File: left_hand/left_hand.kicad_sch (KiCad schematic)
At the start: 4 parts, among them M1 Motor_Servo, Q1 Q_NMOS_GDS, U1 MCP23017_SP

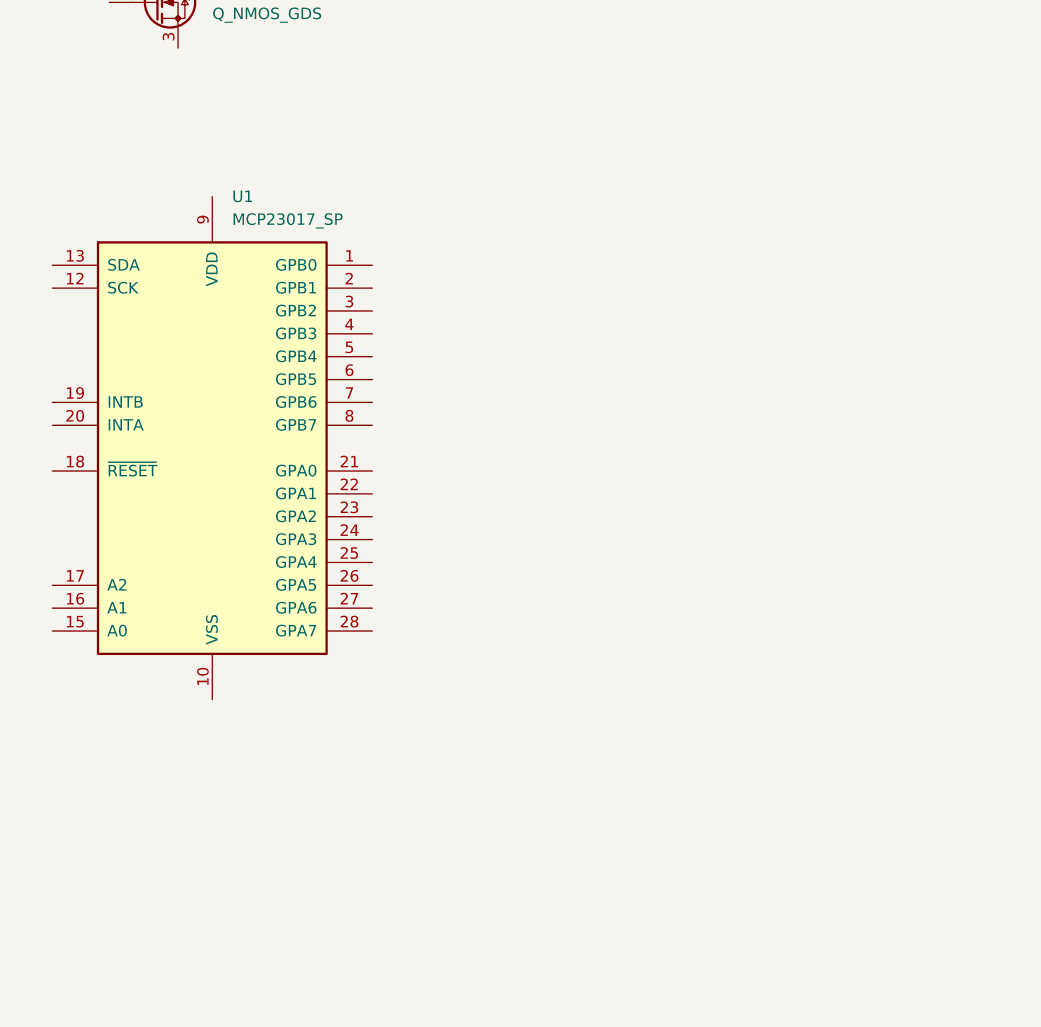
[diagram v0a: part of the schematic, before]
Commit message: Added PCA9615 differential I2C buffer
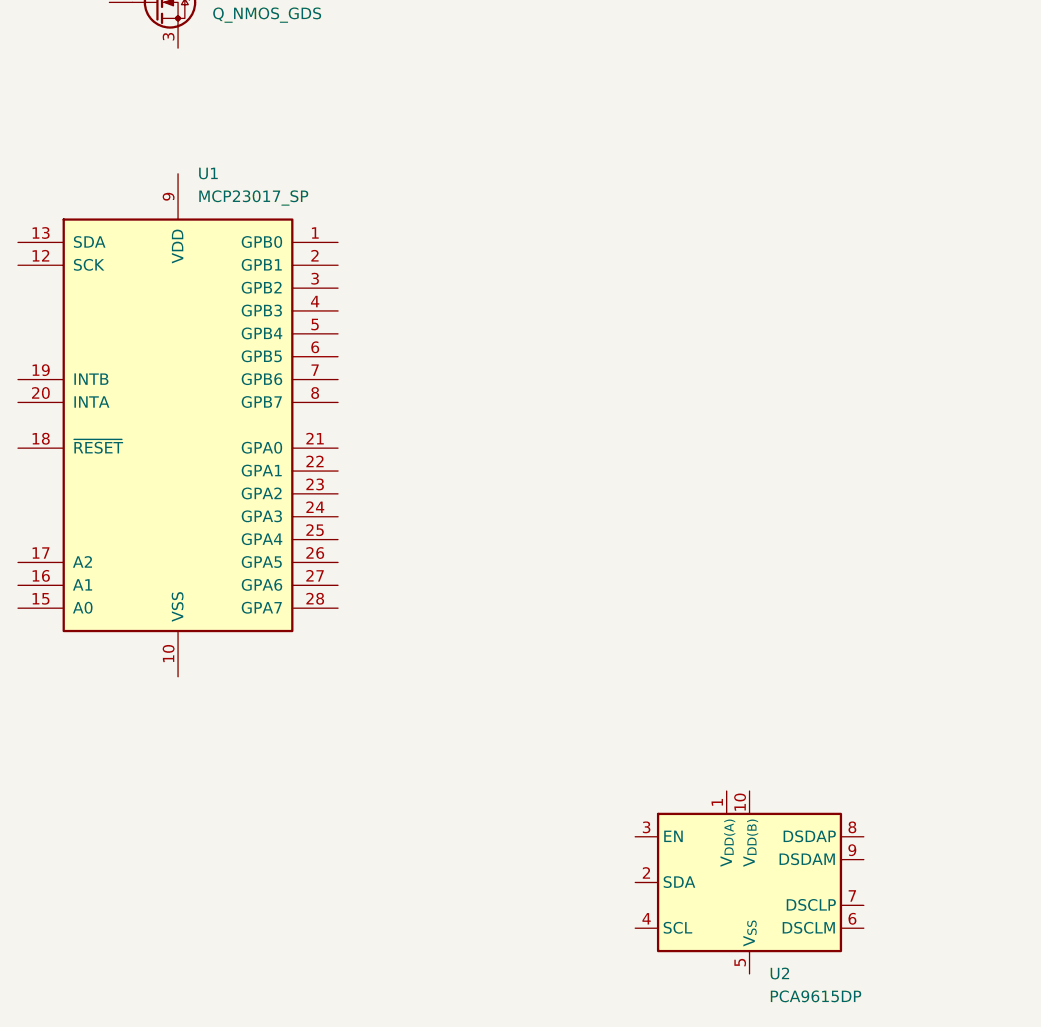
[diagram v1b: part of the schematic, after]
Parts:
- added U2: PCA9615DP, Package_SO:TSSOP-10_3x3mm_P0.5mm, symbol Interface:PCA9615DP
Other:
- moved on the sheet: U1
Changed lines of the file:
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@@
 	(symbol
 		(lib_id "Interface_Expansion:MCP23017_SP")
-		(at 63.5 118.11 0)
+		(at 59.69 115.57 0)
 		(unit 1)
 		(exclude_from_sim no)
@@
 		(fields_autoplaced yes)
 		(property "Reference" "U1"
-			(at 65.6941 90.17 0)
+			(at 61.8841 87.63 0)
 			(effects
 				(font
@@
 		)
 		(property "Value" "MCP23017_SP"
-			(at 65.6941 92.71 0)
+			(at 61.8841 90.17 0)
 			(effects
 				(font
@@
 		)
 		(property "Footprint" "Package_DIP:DIP-28_W7.62mm"
-			(at 68.58 143.51 0)
+			(at 64.77 140.97 0)
 			(effects
 				(font
@@
 		)
 		(property "Datasheet" "http://ww1.microchip.com/downloads/en/DeviceDoc/20001952C.pdf"
-			(at 68.58 146.05 0)
+			(at 64.77 143.51 0)
 			(effects
 				(font
@@
 		)
 		(property "Description" "16-bit I/O expander, I2C, interrupts, w pull-ups, SPDIP-28"
-			(at 63.5 118.11 0)
+			(at 59.69 115.57 0)
 			(effects
 				(font
@@
 		)
 		(property "Digikey" "https://www.digikey.ca/en/products/detail/microchip-technology/MCP23017-E-SP/894272"
-			(at 63.5 118.11 0)
+			(at 59.69 115.57 0)
 			(effects
 				(font
@@
 					(unit 1)
 				)
+			)
+		)
+	)
+	(symbol
+		(lib_id "Interface:PCA9615DP")
+		(at 123.19 166.37 0)
+		(unit 1)
+		(exclude_from_sim no)
+		(in_bom yes)
+		(on_board yes)
+		(dnp no)
+		(fields_autoplaced yes)
+		(property "Reference" "U2"
+			(at 125.3841 176.53 0)
+			(effects
+				(font
+					(size 1.27 1.27)
+				)
+				(justify left)
+			)
+		)
+		(property "Value" "PCA9615DP"
+			(at 125.3841 179.07 0)
+			(effects
+				(font
+					(size 1.27 1.27)
+				)
+				(justify left)
+			)
+		)
+		(property "Footprint" "Package_SO:TSSOP-10_3x3mm_P0.5mm"
+			(at 143.51 175.26 0)
+			(effects
+				(font
+					(size 1.27 1.27)
+				)
+				(hide yes)
+			)
+		)
+		(property "Datasheet" "https://www.nxp.com/docs/en/data-sheet/PCA9615.pdf"
+			(at 123.19 177.8 0)
+			(effects
+				(font
+					(size 1.27 1.27)
+				)
+				(hide yes)
+			)
+		)
+		(property "Description" "Dual bidirectional hot-swap multipoint bus buffer, SO-8"
+			(at 123.19 166.37 0)
+			(effects
+				(font
+					(size 1.27 1.27)
+				)
+				(hide yes)
+			)
+		)
+		(property "Digikey" "https://www.digikey.ca/en/products/detail/nxp-usa-inc/PCA9615DPZ/14635231"
+			(at 123.19 166.37 0)
+			(effects
+				(font
+					(size 1.27 1.27)
+				)
+				(hide yes)
+			)
+		)
+		(pin "9"
+		)
+		(pin "2"
+		)
+		(pin "4"
+		)
+		(pin "7"
+		)
+		(pin "10"
+		)
+		(pin "6"
+		)
+		(pin "3"
+		)
+		(pin "5"
+		)
+		(pin "1"
+		)
+		(pin "8"
+		)
+		(instances
+			(project ""
+				(path "/22d0e2d6-ca63-4bde-b22b-39e933f56b8a"
+					(reference "U2")
+					(unit 1)
+				)

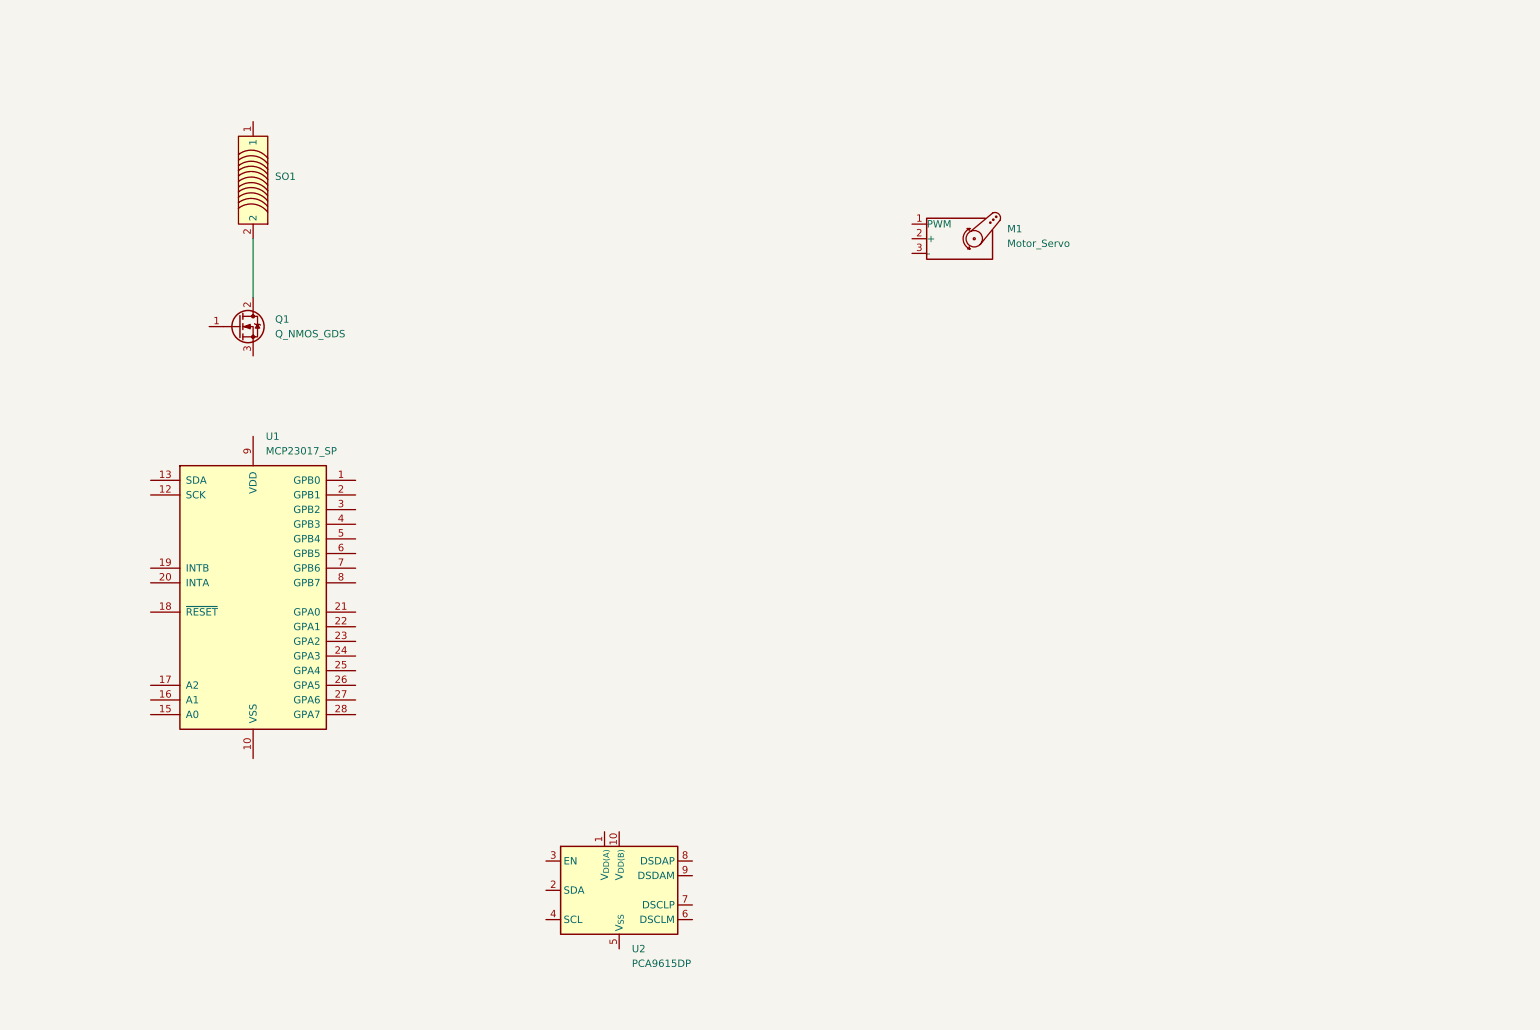
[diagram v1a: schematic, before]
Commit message: Added PCA9685 PWM generator IC
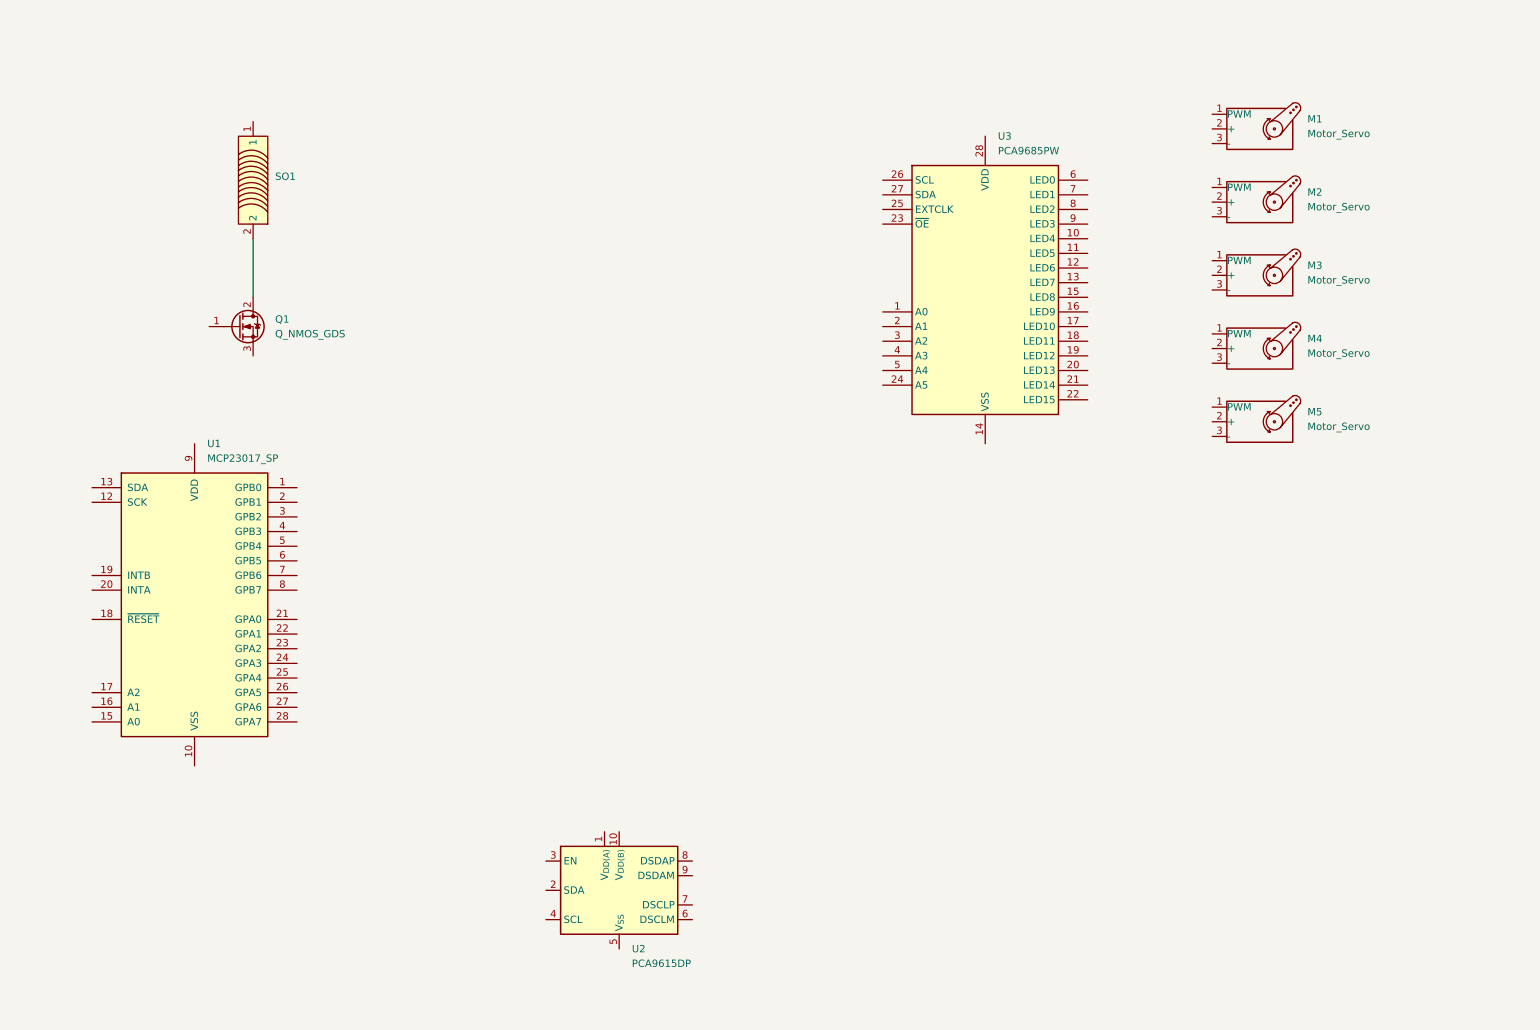
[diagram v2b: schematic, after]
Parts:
- added M2, M3, M4, M5: Motor_Servo, symbol Motor:Motor_Servo
- added U3: PCA9685PW, Package_SO:TSSOP-28_4.4x9.7mm_P0.65mm, symbol Driver_LED:PCA9685PW
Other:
- moved on the sheet: M1, U1

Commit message: Added 12V power rail and regulator
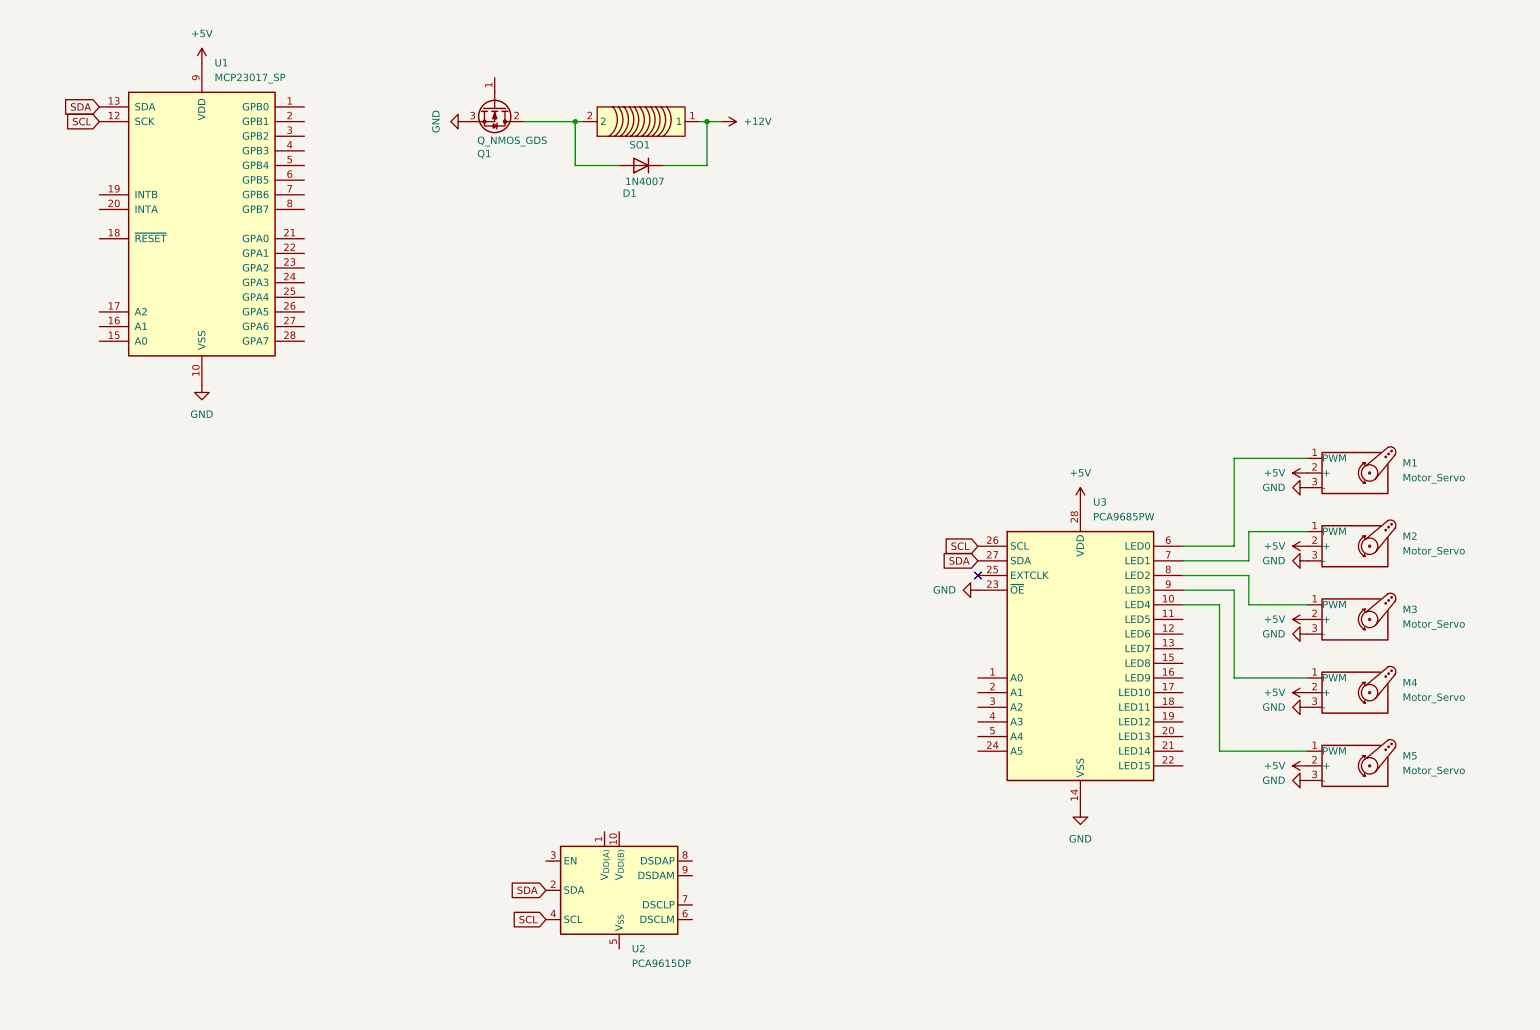
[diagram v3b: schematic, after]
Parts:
- added D1: 1N4007, Diode_THT:D_DO-41_SOD81_P10.16mm_Horizontal, symbol Diode:1N4007
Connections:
- net GND: now reaches U1.10 (VSS)
- net GND: now also M1.3 (-), M2.3 (-), M3.3 (-), M4.3 (-), M5.3 (-), Q1.3 (S), U3.14 (VSS), U3.23 (~{OE})
- net SCL: now reaches U1.12 (SCK)
- net SCL: now also U2.4 (SCL), U3.26 (SCL)
- net SDA: now reaches U1.13 (SDA)
- net SDA: now also U2.2 (SDA), U3.27 (SDA)
- net +5V: now reaches U1.9 (VDD)
- net +5V: now also M1.2 (+), M2.2 (+), M3.2 (+), M4.2 (+), M5.2 (+), U3.28 (VDD)
- net at M3.1 (PWM): now also U3.8 (LED2)
- net at U3.10 (LED4): now also M5.1 (PWM)
- net at U3.6 (LED0): now also M1.1 (PWM)
- net at U3.7 (LED1): now also M2.1 (PWM)
- net at U3.9 (LED3): now also M4.1 (PWM)
- net at Q1.2 (D), SO1.2: now also D1.2 (A)
- net +12V: now reaches SO1.1
- net +12V: now also D1.1 (K)
- no-connect marks 0 -> 1
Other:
- moved on the sheet: M1, M2, M3, M4, M5, Q1, SO1, U1, U3
